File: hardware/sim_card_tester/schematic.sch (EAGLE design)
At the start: 139 parts, among them IC1 TPS6300, J13 U.FL-R-SMT, J2 MICRO_USB_B_HIROSE_ZX62R-B-5P, J3 CON_MICRO_SDDM3AT-SF-PEJM5, J4 NANO_SIM, J5 NANO_SIM, J6 TC2030-JLINK-L, J7 NANO_SIM, J8 NANO_SIM, Q1 MOSFET-NCHANNELSMD, Q2 MOSFET-NCHANNELSMD, Q6 MOSFET-NCHANNELSMD, Q7 SI223DDS, U1 AB1815-T3, U10 SIP32510, U11 SIP32510, U12 UBLOX_SARA_G350, U13 TXB0104RUT, U15 MAX4734EUB+, U2 BGA725L6-ALT, U20 MAX4734EUB+, U21 MAX4734EUB+, U22 MAX4734EUB+, U3 FTDI234XD, U4 SAFFB1G56KB0F0A, U5 MAX8887EZK33+T, U6 MCP73831, U7 MAX-M8, U8 MAX67XXMAX6749MAX67XX, U9 NRF52840, X1 ABS07-32.768KHZ-7-T, X4 32MHz, X5 32.768kHz

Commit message: renumbered
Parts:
- removed C50, C70: 10uF, Nordic_nRF:CAPACITOR_0603_L
- removed C55, C56: 1uF, Nordic_nRF:CAPACITOR_0603_L
- removed C58, C59, C60, C67, C68: 4.7uF, Nordic_nRF:CAPACITOR_0603_L
- removed J13: U.FL-R-SMT, connector:U.FL-R-SMT
- removed L7: 2.2u, Nordic_nRF:INDUCTOR_0201_L
- removed L9: 15nH, passives:INDUCTOR0402
- removed Q6: MOSFET-NCHANNELSMD, fets:MOSFET-NCHANNELSMD
- removed R39: 10k, BeagleBone_Black_Wireless:R-US_R0603
- removed R41: 1M, BeagleBone_Black_Wireless:R-US_R0603
- removed R43, R46: 100k, BeagleBone_Black_Wireless:R-US_R0603
- removed R48: 100, BeagleBone_Black_Wireless:R-US_R0603
- added C13: 56pF, Nordic_nRF:CAPACITOR_0603_L
- added C15: 820pF, Nordic_nRF:CAPACITOR_0603_L
- added C22, C24, C25, C26: 0.1uF, Nordic_nRF:CAPACITOR_0603_L
- added C29: 100nF, Nordic_nRF:CAPACITOR_0603_L
- added C45: 100uF, Nordic_nRF:CAPACITOR_0603_L
- added C46: 220uF, Nordic_nRF:CAPACITOR_0603_L
- added J1: CON_MICRO_SDDM3AT-SF-PEJM5, connector:CON_MICRO_SDDM3AT-SF-PEJM5
- added L5, L6: 1kH, passives:FERRITE_BEAD0402
- added Q3: MOSFET-NCHANNELSMD, fets:MOSFET-NCHANNELSMD
- added R14, R20, R21, R25: 10k, BeagleBone_Black_Wireless:R-US_R0603
- added R36: 1.3M, BeagleBone_Black_Wireless:R-US_R0603
- C1: value 47pF -> 12pF; device passives:CAPACITOR0402_CAP -> Nordic_nRF:CAPACITOR_0603_L; DESCRIPTION CAP CER 47PF 100V C0G/NP0 0402 -> (none); DIGIKEY 490-7307-1-ND -> 490-6197-1-ND; MANUFACTURER Murata Electronics North America -> (none); MPN GRM1555C2A470JA01D -> GRM1555C1H120GA01D
- C10: value 1uF -> 47pF; device passives:CAPACITOR0402_CAP -> Nordic_nRF:CAPACITOR_0603_L; DESCRIPTION CAP CER 1UF 10V X7S 0402 -> CAP CER 47PF 50V C0G/NP0 0402; DIGIKEY 490-13409-1-ND -> 490-6241-1-ND; MANUFACTURER Murata Electronics North America -> Murata; MPN GCM155C71A105KE38D -> GRM1555C1H470FA01D
- C14: value 10uF -> 100pF; DIGIKEY 490-12538-1-ND -> 490-5922-1-ND; MANUFACTURER Murata Electronics -> (none); MPN GRM188R60J106KE47D -> GRM1555C1H101JA01D
- C16: value 47pF -> 10nF; DESCRIPTION CAP CER 47PF 50V C0G/NP0 0402 -> CAP CER 10000PF 16V X7R 0402; DIGIKEY 490-6241-1-ND -> 490-1313-1-ND; MANUFACTURER Murata -> Murata Electronics North America; MPN GRM1555C1H470FA01D -> GRM155R71C103KA01D
- C17: value 56pF -> 10nF; DESCRIPTION CAP CER 56PF 50V C0G/NP0 0402 -> (none); DIGIKEY 490-1288-1-ND -> 490-7194-1-ND; MANUFACTURER Murata -> Murata Electronics; MPN GRM1555C1H560JA01D -> GRM033R61E103KA12D
- C18: value 100uF -> 10nF; DESCRIPTION CAP CER 100UF 6.3V X5R 0805 -> (none); DIGIKEY 490-13981-1-ND -> 490-6296-1-ND; MANUFACTURER Murata -> (none); MPN GRM21BR60J107ME15L -> (none)
- C19: DESCRIPTION CAP CER 10000PF 50V 10% X7R 0402 -> (none); DIGIKEY 490-4516-1-ND -> (none); MANUFACTURER Murata -> (none); MPN GRM155R71H103KA88D -> (none)
- C2: value 10nF -> 12pF; DESCRIPTION CAP CER 10000PF 16V X7R 0402 -> (none); DIGIKEY 490-1313-1-ND -> 490-6197-1-ND; MANUFACTURER Murata Electronics North America -> (none); MPN GRM155R71C103KA01D -> GRM1555C1H120GA01D
- C20: value 220uF -> 10nF; DESCRIPTION CAP CER 220UF 6.3V X5R 1210 -> CAP CER 10000PF 50V 10% X7R 0402; DIGIKEY 1276-3375-1-ND -> 490-4516-1-ND; MANUFACTURER Samsung -> Murata; MPN CL32A227MQVNNNE -> GRM155R71H103KA88D
- C21: value 100nF -> 47nF; DESCRIPTION CAP CER 0.1UF 10V X7R 0402 -> (none); DIGIKEY 490-10777-1-ND -> 445-1264-1-ND; MANUFACTURER Murata -> (none); MPN GRM155R71A104JA01D -> C1005X7R1C473K050BC
- C23: value 100nF -> 0.1uF; DIGIKEY 490-10777-1-ND -> (none)
- C27: value 33pF -> 0.1uF; DESCRIPTION CAP CER 33PF 250V C0G/NP0 0603 -> (none); DIGIKEY 712-1342-1-ND -> (none); MANUFACTURER Johanson -> (none); MPN 251R14S330JV4T -> (none)
- C28: value 47pF -> 100nF; DESCRIPTION CAP CER 47PF 50V C0G/NP0 0402 -> (none); DIGIKEY 490-6241-1-ND -> 490-10777-1-ND; MANUFACTURER Murata -> (none); MPN GRM1555C1H470FA01D -> (none)
- C3: value 10nF -> 12pF; DIGIKEY 490-7194-1-ND -> 490-6197-1-ND; MANUFACTURER Murata Electronics -> (none); MPN GRM033R61E103KA12D -> GRM1555C1H120GA01D
- C30: value 0.1uF -> 0.82uF; DIGIKEY (none) -> 490-10440-1-ND; MANUFACTURER (none) -> Murata Electronics North America; MPN (none) -> GRM155C80J824KE15D
- C31: value 0.1uF -> 1uF; device Nordic_nRF:CAPACITOR_0603_L -> passives:CAPACITOR0402_CAP; DESCRIPTION (none) -> CAP CER 1UF 10V X7S 0402; DIGIKEY 490-6328-1-ND -> 490-13409-1-ND; MANUFACTURER (none) -> Murata Electronics North America; MPN GRM155R71C104KA88J -> GCM155C71A105KE38D
- C32: value 0.1uF -> 1uF; DIGIKEY 490-6328-1-ND -> (none); MPN GRM155R71C104KA88J -> (none)
- C33: value 10nF -> 1uF; DIGIKEY (none) -> 490-7195-1-ND; MPN (none) -> GRM155R70G105KA12D
- C34: value 0.1uF -> 2.2uF; DIGIKEY 490-6328-1-ND -> 490-12696-1-ND; MANUFACTURER (none) -> Murata Electronics North America; MPN GRM155R71C104KA88J -> GRM155C70J225KE11D
- C35: value 0.1uF -> 4.7uF
- C36: value 100pF -> 4.7uF; DIGIKEY 490-5922-1-ND -> (none); MPN GRM1555C1H101JA01D -> (none)
- C37, C38: value 12pF -> 4.7uF; DIGIKEY 490-6197-1-ND -> (none); MPN GRM1555C1H120GA01D -> (none)
- C4: value 10nF -> 12pF; DIGIKEY 490-6296-1-ND -> 490-6197-1-ND; MPN (none) -> GRM1555C1H120GA01D
- C40: value 10uF -> 4.7uF; DESCRIPTION (none) -> CAP CER 4.7UF 6.3V X5R 0402; DIGIKEY (none) -> 445-5947-1-ND; MANUFACTURER (none) -> TDK; MPN (none) -> C1005X5R0J475K050BC
- C41: value 47nF -> 10uF; DIGIKEY 445-1264-1-ND -> 490-12538-1-ND; MANUFACTURER (none) -> Murata Electronics; MPN C1005X7R1C473K050BC -> GRM188R60J106KE47D
- C42, C43: value 12pF -> 10uF; DIGIKEY 490-6197-1-ND -> (none); MPN GRM1555C1H120GA01D -> (none)
- C44: value 820pF -> 10uF; DIGIKEY 1276-6989-1-ND -> (none); MPN CL05C821JB5NFNC -> (none)
- C5: value 47pF -> 33pF; DESCRIPTION (none) -> CAP CER 33PF 250V C0G/NP0 0603; DIGIKEY 490-6241-1-ND -> 712-1342-1-ND; MANUFACTURER (none) -> Johanson; MPN (none) -> 251R14S330JV4T
- C6: device Nordic_nRF:CAPACITOR_0603_L -> passives:CAPACITOR0402_CAP; DESCRIPTION (none) -> CAP CER 47PF 100V C0G/NP0 0402; DIGIKEY 490-6241-1-ND -> 490-7307-1-ND; MANUFACTURER (none) -> Murata Electronics North America; MPN (none) -> GRM1555C2A470JA01D
- C7: value 0.1uF -> 47pF; DIGIKEY 490-5405-1-ND -> 490-6241-1-ND; MANUFACTURER Murata Electronics -> (none); MPN GRM033R61A104ME15D -> (none)
- C8: value 2.2uF -> 47pF; DIGIKEY 490-12696-1-ND -> 490-6241-1-ND; MANUFACTURER Murata Electronics North America -> (none); MPN GRM155C70J225KE11D -> (none)
- C9: value 0.82uF -> 47pF; DESCRIPTION (none) -> CAP CER 47PF 50V C0G/NP0 0402; DIGIKEY 490-10440-1-ND -> 490-6241-1-ND; MANUFACTURER Murata Electronics North America -> Murata; MPN GRM155C80J824KE15D -> GRM1555C1H470FA01D
- J3: value CON_MICRO_SDDM3AT-SF-PEJM5 -> NANO_SIM; device connector:CON_MICRO_SDDM3AT-SF-PEJM5 -> signpost:NANO_SIM
- J6: value TC2030-JLINK-L -> NANO_SIM; device connector:TC2030-JLINK-L -> signpost:NANO_SIM
- J7: value NANO_SIM -> TC2030-JLINK-L; device signpost:NANO_SIM -> connector:TC2030-JLINK-L
- J8: value NANO_SIM -> U.FL-R-SMT; device signpost:NANO_SIM -> connector:U.FL-R-SMT
- L2: value 1k -> 15nH; device passives:FERRITE_BEAD0402 -> passives:INDUCTOR0402; DESCRIPTION FERRITE BEAD 1 KOHM 0402 1LN -> (none); DIGIKEY 490-4003-1-ND -> 587-1521-1-ND; MANUFACTURER Murata -> (none); MPN BLM15HD102SN1D -> HK100515NJ-T
- L3: value 1k -> 2.2uH; device passives:FERRITE_BEAD0402 -> Nordic_nRF:INDUCTOR_0201_L; DESCRIPTION FERRITE BEAD 1 KOHM 0402 1LN -> (none); DIGIKEY 490-4003-1-ND -> (none); MANUFACTURER Murata -> (none); MPN BLM15HD102SN1D -> (none)
- R1, R2: value 27Ω -> 27
- R10: value 10k -> 1k; DESCRIPTION RES SMD 10K OHM 5% 1/16W 0402 -> RES SMD 1K OHM 1% 1/16W 0402; DIGIKEY 311-10KJRCT-ND -> RMCF0402FT1K00CT-ND; MANUFACTURER Yageo -> Stackpole Electronics; MPN RC0402JR-0710KL -> RMCF0402FT1K00
- R11: DESCRIPTION RES SMD 1K OHM 5% 1/16W 0402 -> (none); DIGIKEY 311-1.0KJRCT-ND -> (none); MANUFACTURER Yageo -> (none); MPN RC0402JR-071KL -> (none)
- R12: value 100k -> 1k; DESCRIPTION RES SMD 100K OHM 1% 1/16W 0402 -> RES SMD 1K OHM 5% 1/16W 0402; DIGIKEY 311-100KLRCT-ND -> 311-1.0KJRCT-ND; MPN RC0402FR-07100KL -> RC0402JR-071KL
- R13: value 10M -> 2k
- R18: DESCRIPTION RES SMD 10K OHM 1% 1/16W 0402 -> (none); DIGIKEY RMCF0402FT10K0CT-ND -> (none); MANUFACTURER Stackpole Electronics Inc. -> (none); MPN RMCF0402FT10K0 -> (none)
- R19: value 2.2M -> 10k
- R22: value 100k -> 10k; DESCRIPTION RES SMD 100K OHM 1% 1/16W 0402 -> (none); DIGIKEY 541-100KLCT-ND -> (none); MANUFACTURER Vishay Dale -> (none); MPN CRCW0402100KFKED -> (none)
- R23: value 100 -> 10k
- R26: value 1.3M -> 100k; DESCRIPTION (none) -> RES SMD 100K OHM 1% 1/16W 0402; DIGIKEY (none) -> 541-100KLCT-ND; MANUFACTURER (none) -> Vishay Dale; MPN (none) -> CRCW0402100KFKED
- R27: value 499k -> 100k; DESCRIPTION RES SMD 499K OHM 1% 1/10W 0402 -> (none); DIGIKEY P499KLCT-ND -> (none); MANUFACTURER Panasonic Electronic Components -> (none); MPN ERJ-2RKF4993X -> (none)
- R28: value 200k -> 100k
- R29, R30, R31: value 470 -> 100k; DESCRIPTION (none) -> RES SMD 100K OHM 1% 1/16W 0402; DIGIKEY (none) -> 311-100KLRCT-ND; MANUFACTURER (none) -> Yageo; MPN (none) -> RC0402FR-07100KL
- R3, R4: value 100Ω -> 100
- R32: value 825k -> 200k; DESCRIPTION RES SMD 825K OHM 1% 1/10W 0402 -> (none); DIGIKEY P825KLCT-ND -> (none); MANUFACTURER Panasonic Electronic Components -> (none); MPN ERJ-2RKF8253X -> (none)
- R33: value 10k -> 499k; DESCRIPTION (none) -> RES SMD 499K OHM 1% 1/10W 0402; DIGIKEY (none) -> P499KLCT-ND; MANUFACTURER (none) -> Panasonic Electronic Components; MPN (none) -> ERJ-2RKF4993X
- R34: value 10k -> 825k; DESCRIPTION (none) -> RES SMD 825K OHM 1% 1/10W 0402; DIGIKEY (none) -> P825KLCT-ND; MANUFACTURER (none) -> Panasonic Electronic Components; MPN (none) -> ERJ-2RKF8253X
- R35: value 10k -> 1M; DESCRIPTION (none) -> RES 1M OHM 1% 1/16W 0402; DIGIKEY (none) -> RMCF0402FT1M00CT-ND; MANUFACTURER (none) -> Stackpole Electronics Inc.; MPN (none) -> RMCF0402FT1M00
- R37: value 10k -> 2.2M
- R38: value 10k -> 10M
- R5: value 1k -> 100; DESCRIPTION RES SMD 1K OHM 1% 1/16W 0402 -> (none); DIGIKEY RMCF0402FT1K00CT-ND -> (none); MANUFACTURER Stackpole Electronics -> (none); MPN RMCF0402FT1K00 -> (none)
- R6: value 100k -> 100; DESCRIPTION (none) -> RES SMD 100 OHM 1% 1/16W 0402; DIGIKEY (none) -> 311-100LRCT-ND; MANUFACTURER (none) -> Yageo; MPN (none) -> RC0402FR-07100RL
- R7: value 100k -> 470
- R8: value 1k -> 470
- R9: value 2k 1% -> 470
- renumbered C61 to C39, FB2 to FB1, L10 to L4, LED2 to LED1, Q7 to Q4
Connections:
- net !CHRG: now also R11.1; no longer R8.1
- net !EXTERNAL_RST: now also R16.2; no longer R17.2
- net !NRF_CS_SD: now also J1.DATA3-CD/CS_N, R19.1; no longer J3.DATA3-CD/CS_N, R34.1
- net !NRF_RST: now also J7.!RESET; no longer J6.!RESET
- net !RTC_CS: now also R15.2, R17.2; no longer R16.2, R18.2
- net !RTC_INT1: now also R14.2; no longer R15.2
- net !SD_DETECT: now also J1.A, R28.1; no longer J3.A, R7.1
- net +3V3: now also C24.1, C26.1, C27.1, C32.1, C37.1, C38.1, C43.1, C44.1, J7.VCC, R11.2, R14.1, R25.2, R35.1, R36.2; no longer C10.1, C34.1, C40.1, C50.1, C55.1, C58.1, C59.1, C67.1, J6.VCC, R10.2, R16.1, R26.2, R41.1, R8.2
- net BAT: now also C36.1, C42.1, R16.1, R34.1, R38.2, R5.2; no longer C68.1, C70.1, R13.2, R17.1, R23.2, R32.1
- net BATIN: now also C23.2, R37.2, R38.1; no longer C30.2, R13.1, R19.2
- net CLK1: now also J3.C3(CLK); no longer J4.C3(CLK)
- net CLK2: now also J4.C3(CLK); no longer J5.C3(CLK)
- net CLK3: now also J5.C3(CLK); no longer J7.C3(CLK)
- net CLK4: now also J6.C3(CLK); no longer J8.C3(CLK)
- net CLK_SIM: now also C12.1; no longer C28.1
- net D+: now also C8.1; no longer C6.1
- net D-: now also C7.1; no longer C5.1
- net GND: now also C1.1, C13.2, C14.2, C15.2, C16.1, C17.1, C22.1, C23.1, C24.2, C25.2, C26.2, C27.2, C28.2, C29.2, C30.2, C37.2, C38.2, C4.1, C41.1, C42.2, C43.2, C45.2, C46.2, C7.2, J1.B, J1.GND, J3.C5(GND), J6.C5(GND), J7.GND, J8.P$2, Q3.S, R13.1, R26.1, R30.1, R31.1, R32.1, R33.2, R37.1; no longer C1.2, C10.2, C14.1, C17.2, C23.2, C30.1, C37.1, C38.1, C4.2, C41.2, C42.1, C43.1, C5.2, C50.2, C55.2, C56.2, C58.2, C59.2, C60.2, C67.2, C68.2, C7.1, C70.2, C9.2, J13.P$2, J3.B, J3.GND, J6.GND, J7.C5(GND), J8.C5(GND), Q6.S, R12.1, R19.1, R22.1, R28.1, R46.1, R6.2, R9.1
- net GPS_PWR_EN: now also R26.2; no longer R22.2
- net GPS_RXD: now also L6.P$2; no longer L3.P$2
- net GPS_TXD: now also L5.P$2; no longer L2.P$2
- net GPS_VCC: now also C17.2, C22.2, C41.2, R10.2; no longer C14.2, C3.2, C7.2, R5.2
- net GSM_GATED: now also C13.1, C29.1, C46.1, R12.2; no longer C17.1, C19.1, C21.1, R11.2
- net GSM_LED: now also Q3.G, R31.2; no longer Q1.G, R12.2
- net GSM_POWER: now also Q1.G; no longer Q2.G
- net GSM_POWER_GATE: now also R30.2, R6.2; no longer R46.2, R48.2
- net GSM_RST: now also Q2.G; no longer Q6.G
- net IO1: now also J3.C7(IO); no longer J4.C7(IO)
- net IO2: now also J4.C7(IO); no longer J5.C7(IO)
- net IO3: now also J5.C7(IO); no longer J7.C7(IO)
- net IO4: now also J6.C7(IO); no longer J8.C7(IO)
- net IO_SIM: now also C9.1; no longer C11.1
- net LED_NRF_BLUE: now also R9.2; no longer R31.2
- net LED_NRF_GREEN: now also R8.2; no longer R30.2
- net LED_NRF_RED: now also R7.2; no longer R29.2
- net MUX_EN: now also R21.2, R22.2, R23.2; no longer R37.2, R38.2, R39.2
- net N$1: now also R10.1; no longer R5.1
- net N$13: now also C6.1; no longer C1.1
- net N$14: now also Q3.D; no longer Q1.D
- net N$15: now also Q2.D; no longer Q6.D
- net N$16: now also C45.1, R29.2; no longer C18.1, R43.2
- net N$17: now also R13.2; no longer R9.2
- net N$18: now also Q1.D, R29.1; no longer Q2.D, R43.1
- net N$22: now also L3.1; no longer L7.1
- net N$23: now also R12.1; no longer R11.1
- net N$26: now also L3.2; no longer L7.2
- net N$27: now also C25.1; no longer C32.1
- net N$28: now also C18.1; no longer C4.1
- net N$29: now also R5.1; no longer R23.1
- net N$31: now also R33.1, R34.2, R35.2; no longer R27.1, R32.2, R41.2
- net N$32: now also C21.1, C33.1, L2.1; no longer C41.1, C56.1, L9.1
- net N$33: now also R32.2, R36.1; no longer R26.1, R28.2
- net N$34: now also C14.1; no longer C36.1
- net N$35: now also C19.1; no longer C33.1
- net N$36: now also C30.1; no longer C9.1
- net N$39: now also C34.1; no longer C8.1
- net N$40: now also L5.P$1; no longer L2.P$1
- net N$41: now also L6.P$1; no longer L3.P$1
- net N$43: now also C1.2; no longer C37.2
- net N$45: now also C2.2; no longer C38.2
- net N$47: now also L2.2; no longer L9.2
- net N$48: now also C15.1; no longer C44.1
- net N$5: now also R17.1; no longer R18.1
- net N$55: now also C40.1, J1.VCC, R18.2, R19.2, R20.2, R28.2; no longer C60.1, J3.VCC, R33.2, R34.2, R35.2, R7.2
- net N$59: now also R7.1; no longer R29.1
- net N$60: now also R8.1; no longer R30.1
- net N$61: now also R9.1; no longer R31.1
- net N$66: now also R6.1; no longer R48.1
- net N$68: now also R25.1; no longer R10.1
- net N$69: now also C5.1; no longer C27.1
- net N$70: now also C5.2, J8.ANT; no longer C27.2, J13.ANT
- net N$71: now also C10.2, C9.2; no longer C16.2, C28.2
- net NRF_MISO: now also J1.DATA0/MISO, R20.1; no longer J3.DATA0/MISO, R35.1
- net NRF_MOSI: now also J1.CMD/MOSI, R18.1; no longer J3.CMD/MOSI, R33.1
- net NRF_SCK: now also J1.CLK; no longer J3.CLK
- net NRF_SWDCLK: now also J7.SWDCLK; no longer J6.SWDCLK
- net NRF_SWDIO: now also J7.SWDIO; no longer J6.SWDIO
- net RST1: now also J3.C2(RST); no longer J4.C2(RST)
- net RST2: now also J4.C2(RST); no longer J5.C2(RST)
- net RST3: now also J5.C2(RST); no longer J7.C2(RST)
- net RST4: now also J6.C2(RST); no longer J8.C2(RST)
- net RST_SIM: now also C10.1; no longer C12.1
- net SD_EN: now also R27.1; no longer R6.1
- net VCC1: now also J3.C1(VCC), R24.1; no longer J4.C1(VCC), R39.1
- net VCC2: now also J4.C1(VCC), R23.1; no longer J5.C1(VCC), R38.1
- net VCC3: now also J5.C1(VCC), R22.1; no longer J7.C1(VCC), R37.1
- net VCC4: now also J6.C1(VCC), R21.1; no longer J8.C1(VCC), R24.1
- net VCC_LINUX_1V8: now also C28.1; no longer C23.1
- net VCC_RF: now also C16.2; no longer C2.2
- net VCC_SIM: now also C11.1; no longer C16.1
- net XL3: now also C4.2; no longer C43.2
- net XL4: now also C3.2; no longer C42.2

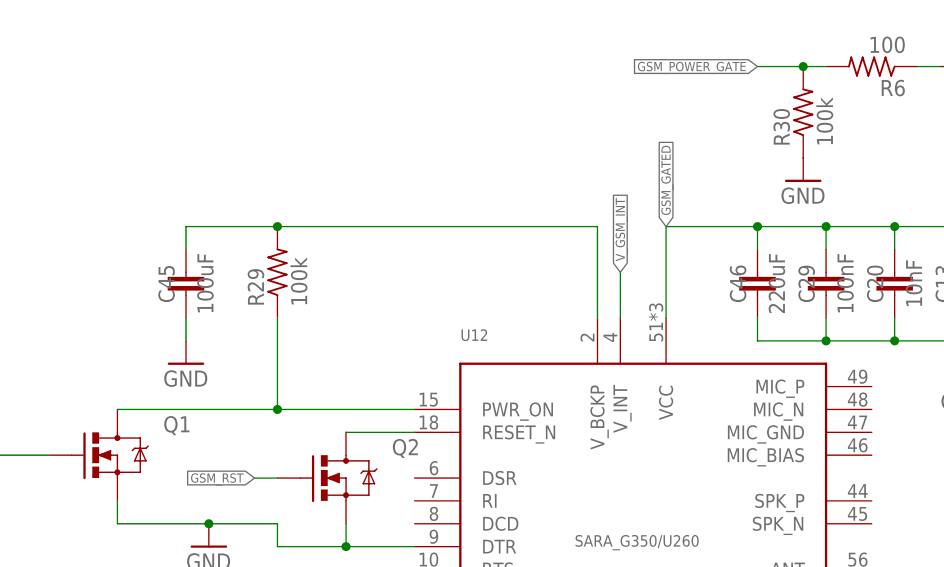
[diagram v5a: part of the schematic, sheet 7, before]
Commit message: updated parts for caps
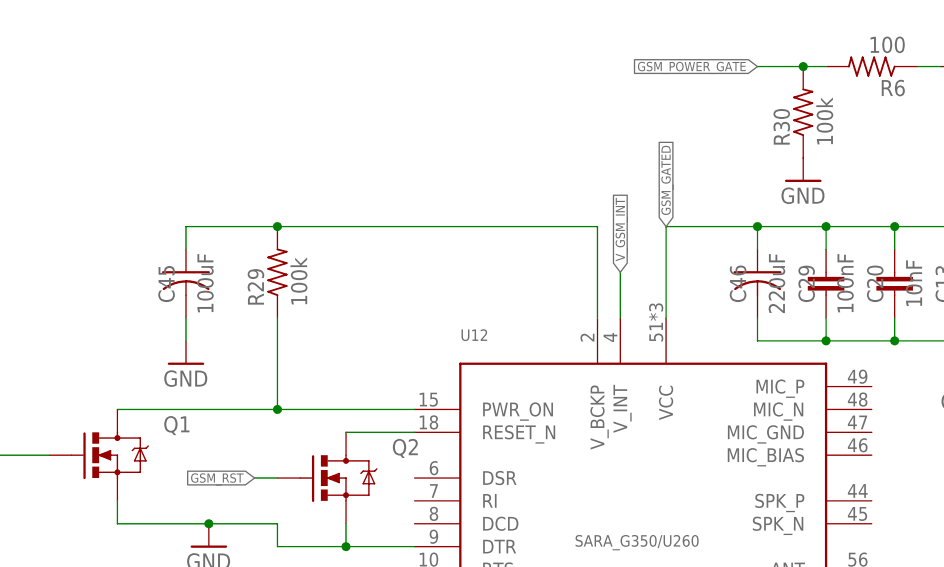
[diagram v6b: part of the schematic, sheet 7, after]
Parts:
- C1, C2, C3, C4: DIGIKEY 490-6197-1-ND -> 311-1059-1-ND; MANUFACTURER (none) -> Yageo; MPN GRM1555C1H120GA01D -> CC0603JRNPO9BN120
- C10, C11, C12, C9: DESCRIPTION CAP CER 47PF 50V C0G/NP0 0402 -> (none); DIGIKEY 490-6241-1-ND -> 311-1065-1-ND; MANUFACTURER Murata -> Yageo; MPN GRM1555C1H470FA01D -> CC0603JRNPO9BN470
- C13: DESCRIPTION CAP CER 56PF 50V C0G/NP0 0402 -> (none); DIGIKEY 490-1288-1-ND -> 311-1066-1-ND; MANUFACTURER Murata -> Yageo; MPN GRM1555C1H560JA01D -> CC0603JRNPO9BN560
- C14: DIGIKEY 490-5922-1-ND -> 311-1069-1-ND; MANUFACTURER (none) -> Yageo; MPN GRM1555C1H101JA01D -> CC0603JRNPO9BN101
- C15: DIGIKEY 1276-6989-1-ND -> 311-1189-1-ND; MANUFACTURER (none) -> Yageo; MPN CL05C821JB5NFNC -> CC0603KRX7R9BB821
- C16: DESCRIPTION CAP CER 10000PF 16V X7R 0402 -> (none); DIGIKEY 490-1313-1-ND -> 490-7194-1-ND; MANUFACTURER Murata Electronics North America -> Murata Electronics; MPN GRM155R71C103KA01D -> GRM033R61E103KA12D; SPICEPREFIX (none) -> C
- C18: DIGIKEY 490-6296-1-ND -> 490-7194-1-ND; MANUFACTURER (none) -> Murata Electronics; MPN (none) -> GRM033R61E103KA12D
- C19: DIGIKEY (none) -> 490-7194-1-ND; MANUFACTURER (none) -> Murata Electronics; MPN (none) -> GRM033R61E103KA12D
- C20: DESCRIPTION CAP CER 10000PF 50V 10% X7R 0402 -> (none); DIGIKEY 490-4516-1-ND -> 490-7194-1-ND; MANUFACTURER Murata -> Murata Electronics; MPN GRM155R71H103KA88D -> GRM033R61E103KA12D
- C21: DIGIKEY 445-1264-1-ND -> 490-5854-1-ND; MANUFACTURER (none) -> Murata Electronics; MPN C1005X7R1C473K050BC -> GCJ188R71H473KA12D
- C28: DIGIKEY 490-10777-1-ND -> 490-5405-1-ND; MANUFACTURER (none) -> Murata Electronics; MPN (none) -> GRM033R61A104ME15D
- C30: DIGIKEY 490-10440-1-ND -> 399-3117-1-ND; MANUFACTURER Murata Electronics North America -> KEMET; MPN GRM155C80J824KE15D -> C0603C824K8PACTU
- C31: DESCRIPTION CAP CER 1UF 10V X7S 0402 -> (none); DIGIKEY 490-13409-1-ND -> 399-3118-1-ND; MANUFACTURER Murata Electronics North America -> KEMET; MPN GCM155C71A105KE38D -> C0603C105K8PACTU
- C34: DIGIKEY 490-12696-1-ND -> 490-12738-1-ND; MANUFACTURER Murata Electronics North America -> Murata Electronics; MPN GRM155C70J225KE11D -> GRM188R61E225MA12D
- C35, C36, C37, C38, C39: DIGIKEY (none) -> 490-10992-1-ND; MANUFACTURER (none) -> Murata Electronics; MPN (none) -> ZRB18AR6YA475KE05L
- C40: DESCRIPTION CAP CER 4.7UF 6.3V X5R 0402 -> (none); DIGIKEY 445-5947-1-ND -> 490-10992-1-ND; MANUFACTURER TDK -> Murata Electronics; MPN C1005X5R0J475K050BC -> ZRB18AR6YA475KE05L
- C41: DIGIKEY 490-12538-1-ND -> 490-14372-1-ND
- C42, C43, C44: DIGIKEY (none) -> 490-12538-1-ND; MANUFACTURER (none) -> Murata Electronics; MPN (none) -> GRM188R60J106KE47D
- C45: device Nordic_nRF:CAPACITOR_0603_L -> BeagleBone_Black_Wireless:C-USC1210; DESCRIPTION CAP CER 100UF 6.3V X5R 0805 -> (none); DIGIKEY 490-13981-1-ND -> 490-9969-1-ND; MANUFACTURER Murata -> Murata Electronics; MPN GRM21BR60J107ME15L -> GRM32ER61A107ME20L
- C46: device Nordic_nRF:CAPACITOR_0603_L -> BeagleBone_Black_Wireless:C-USC1210; DESCRIPTION CAP CER 220UF 6.3V X5R 1210 -> (none); DIGIKEY 1276-3375-1-ND -> 490-16308-1-ND; MANUFACTURER Samsung -> Murata Electronics; MPN CL32A227MQVNNNE -> GRM32ER60J227ME05L
- C5: DESCRIPTION CAP CER 33PF 250V C0G/NP0 0603 -> (none); DIGIKEY 712-1342-1-ND -> 399-7896-1-ND; MANUFACTURER Johanson -> KEMET; MPN 251R14S330JV4T -> C0603C330J1GACTU
- C6: DESCRIPTION CAP CER 47PF 100V C0G/NP0 0402 -> (none); DIGIKEY 490-7307-1-ND -> 311-1065-1-ND; MANUFACTURER Murata Electronics North America -> Yageo; MPN GRM1555C2A470JA01D -> CC0603JRNPO9BN470
- C7, C8: DIGIKEY 490-6241-1-ND -> 311-1065-1-ND; MANUFACTURER (none) -> Yageo; MPN (none) -> CC0603JRNPO9BN470

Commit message: parts for resistors
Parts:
- R1, R2: DIGIKEY 1276-3907-1-ND -> 311-27GRCT-ND; MANUFACTURER (none) -> Yageo; MPN (none) -> RC0603JR-0727RL
- R10: DESCRIPTION RES SMD 1K OHM 1% 1/16W 0402 -> (none); DIGIKEY RMCF0402FT1K00CT-ND -> 311-1.0KGRCT-ND; MANUFACTURER Stackpole Electronics -> Yageo; MPN RMCF0402FT1K00 -> RC0603JR-071KL
- R11: DIGIKEY (none) -> 311-1.0KGRCT-ND; MANUFACTURER (none) -> Yageo; MPN (none) -> RC0603JR-071KL
- R12: DESCRIPTION RES SMD 1K OHM 5% 1/16W 0402 -> (none); DIGIKEY 311-1.0KJRCT-ND -> 311-1.0KGRCT-ND; MPN RC0402JR-071KL -> RC0603JR-071KL
- R13: DIGIKEY (none) -> 311-2.00KHRCT-ND; MANUFACTURER (none) -> Yageo; MPN (none) -> RC0603FR-072KL
- R14, R15, R16, R17: DESCRIPTION RES SMD 10K OHM 1% 1/16W 0402 -> (none); DIGIKEY RMCF0402FT10K0CT-ND -> 311-10KGRCT-ND; MANUFACTURER Stackpole Electronics Inc. -> Yageo; MPN RMCF0402FT10K0 -> RC0603JR-0710KL
- R18, R19, R20, R21, R22, R23, R24: DIGIKEY (none) -> 311-10KGRCT-ND; MANUFACTURER (none) -> Yageo; MPN (none) -> RC0603JR-0710KL
- R25: DESCRIPTION RES SMD 10K OHM 5% 1/16W 0402 -> (none); DIGIKEY 311-10KJRCT-ND -> 311-10KGRCT-ND; MPN RC0402JR-0710KL -> RC0603JR-0710KL
- R26: DESCRIPTION RES SMD 100K OHM 1% 1/16W 0402 -> (none); DIGIKEY 541-100KLCT-ND -> 311-100KGRCT-ND; MANUFACTURER Vishay Dale -> Yageo; MPN CRCW0402100KFKED -> RC0603JR-07100KL
- R27, R28: DIGIKEY (none) -> 311-100KGRCT-ND; MANUFACTURER (none) -> Yageo; MPN (none) -> RC0603JR-07100KL
- R29, R30, R31: DESCRIPTION RES SMD 100K OHM 1% 1/16W 0402 -> (none); DIGIKEY 311-100KLRCT-ND -> 311-100KGRCT-ND; MPN RC0402FR-07100KL -> RC0603JR-07100KL
- R3, R4: DIGIKEY 1276-3429-1-ND -> 311-100HRCT-ND; MANUFACTURER (none) -> Yageo; MPN (none) -> RC0603FR-07100RL
- R32: DIGIKEY (none) -> 311-200KGRTR-ND; MANUFACTURER (none) -> Yageo; MPN (none) -> RC0603JR-07200KL
- R33: DESCRIPTION RES SMD 499K OHM 1% 1/10W 0402 -> (none); DIGIKEY P499KLCT-ND -> 311-499KHRCT-ND; MANUFACTURER Panasonic Electronic Components -> Yageo; MPN ERJ-2RKF4993X -> RC0603FR-07499KL
- R34: DESCRIPTION RES SMD 825K OHM 1% 1/10W 0402 -> (none); DIGIKEY P825KLCT-ND -> 311-825KHRCT-ND; MANUFACTURER Panasonic Electronic Components -> Yageo; MPN ERJ-2RKF8253X -> RC0603FR-07825KL
- R35: DESCRIPTION RES 1M OHM 1% 1/16W 0402 -> (none); DIGIKEY RMCF0402FT1M00CT-ND -> 311-1.00MHRCT-ND; MANUFACTURER Stackpole Electronics Inc. -> Yageo; MPN RMCF0402FT1M00 -> RC0603FR-071ML
- R36: DIGIKEY (none) -> YAG3326CT-ND; MANUFACTURER (none) -> Yageo; MPN (none) -> RC0603FR-071M3L
- R37: DIGIKEY (none) -> 311-2.2MGRCT-ND; MANUFACTURER (none) -> Yageo; MPN (none) -> RC0603JR-072M2L
- R38: DIGIKEY (none) -> 311-10MGRCT-ND; MANUFACTURER (none) -> Yageo; MPN (none) -> RC0603JR-0710ML
- R5: DIGIKEY (none) -> 311-100HRCT-ND; MANUFACTURER (none) -> Yageo; MPN (none) -> RC0603FR-07100RL
- R6: DESCRIPTION RES SMD 100 OHM 1% 1/16W 0402 -> (none); DIGIKEY 311-100LRCT-ND -> 311-100HRCT-ND; MPN RC0402FR-07100RL -> RC0603FR-07100RL
- R7, R8, R9: DIGIKEY (none) -> 311-470HRCT-ND; MANUFACTURER (none) -> Yageo; MPN (none) -> RC0603FR-07470RL

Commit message: added most of the parts
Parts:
- J1: MANUFACTOR (none) -> Hirose Electric Co Ltd; MPN (none) -> DM3AT-SF-PEJM5
- L1: device passives:INDUCTOR0402 -> Nordic_nRF:INDUCTOR_0603_M; DESCRIPTION FIXED IND 5.6NH 1.77A 40 MOHM -> (none); DIGIKEY 490-11766-1-ND -> 490-15723-1-ND; MANUFACTURER Murata -> Murata Electronics; MPN LQW15AN5N6B80D -> LQW18AN5N6G8ZD
- L2: device passives:INDUCTOR0402 -> Nordic_nRF:INDUCTOR_0603_M; DIGIKEY 587-1521-1-ND -> 490-15648-1-ND; MANUFACTURER (none) -> Murata Electronics; MPN HK100515NJ-T -> LQW18AN15NG8ZD
- L3: device Nordic_nRF:INDUCTOR_0201_L -> Nordic_nRF:INDUCTOR_0603_M; DIGIKEY (none) -> 490-14478-1-ND; MANUFACTURER (none) -> Murata Electronics; MPN (none) -> LQM18PN2R2MGHD
- L4: device passives:INDUCTOR0603 -> Nordic_nRF:INDUCTOR_0603_M; DIGIKEY 490-4025-1-ND -> 587-1720-1-ND; MANUFACTURER (none) -> Taiyo Yuden; MPN LQM18FN100M00D -> CBMF1608T100K
- L5, L6: value 1kH -> 1k; device passives:FERRITE_BEAD0402 -> Nordic_nRF:INDUCTOR_0603_M; DESCRIPTION FERRITE BEAD 1 KOHM 0402 1LN -> (none); DIGIKEY 490-4003-1-ND -> 490-1015-1-ND; MANUFACTURER Murata -> BLM18AG102SN1D; MPN BLM15HD102SN1D -> Murata Electronics
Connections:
- removed net N$40: L5.P$1, U7.TXD
- removed net N$41: L6.P$1, U7.RXD
- new net N$7: L5.1, U7.TXD
- new net N$8: L6.1, U7.RXD
- net GPS_RXD: now also L6.2; no longer L6.P$2
- net GPS_TXD: now also L5.2; no longer L5.P$2
